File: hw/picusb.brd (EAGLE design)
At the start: 44.5 x 31.8 mm, 38 parts, among them Q1 BSS138, Q2 BSS138, Q3 BSS84, Q4 BSS84, U1 PIC16F1454SOIC, U2 AP7115W, X1 MINI-USB-UX60-MB-5ST

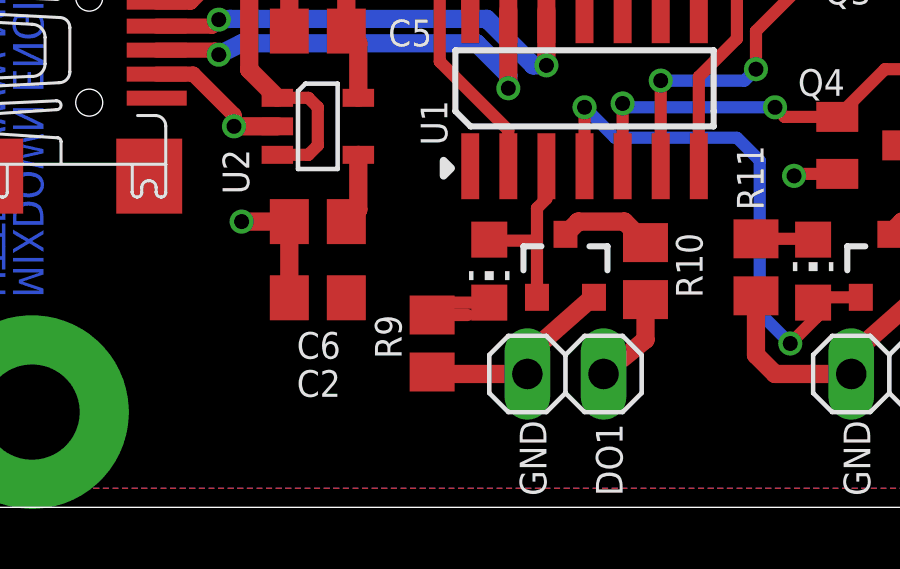
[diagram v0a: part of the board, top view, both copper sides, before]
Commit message: remove extra trace
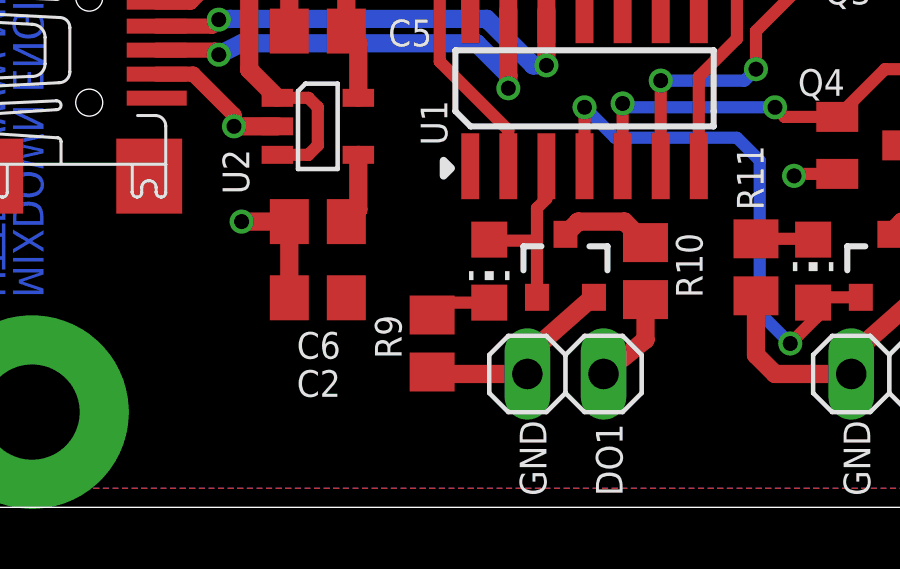
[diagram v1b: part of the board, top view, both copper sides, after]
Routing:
- net N$8: track 3.51 -> 2.32 mm
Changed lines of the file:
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@@
 <signal name="N$8">
 <contactref element="R9" pad="2"/>
-<wire x1="17.702" y1="6.411" x2="16.51" y2="6.411" width="0.4064" layer="1"/>
 <contactref element="LED1" pad="C"/>
 <wire x1="18.415" y1="6.824" x2="16.51" y2="6.824" width="0.4064" layer="1"/>
